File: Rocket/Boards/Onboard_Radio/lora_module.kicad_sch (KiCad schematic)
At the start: 30 parts, among them J11 RFIO SMA, U1 SX1262IMLTRT, U6 PE4259 RF Switch, Y2 Crystal

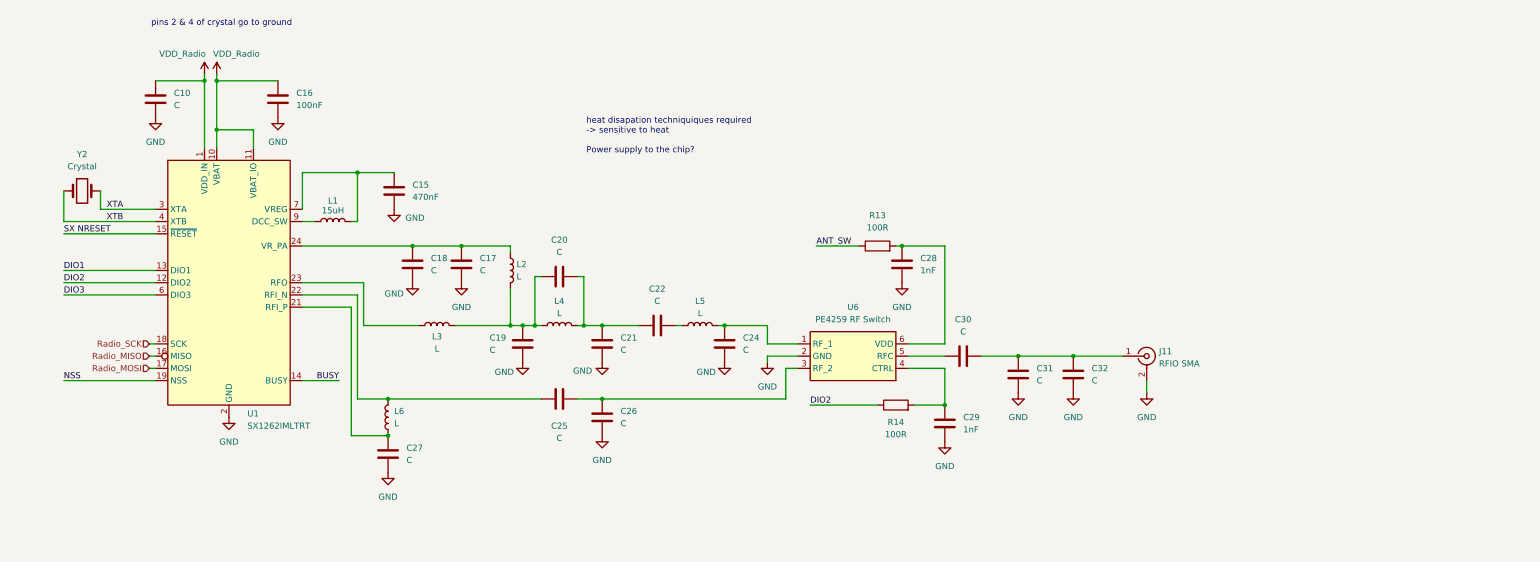
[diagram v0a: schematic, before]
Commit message: rf chip schematic changed
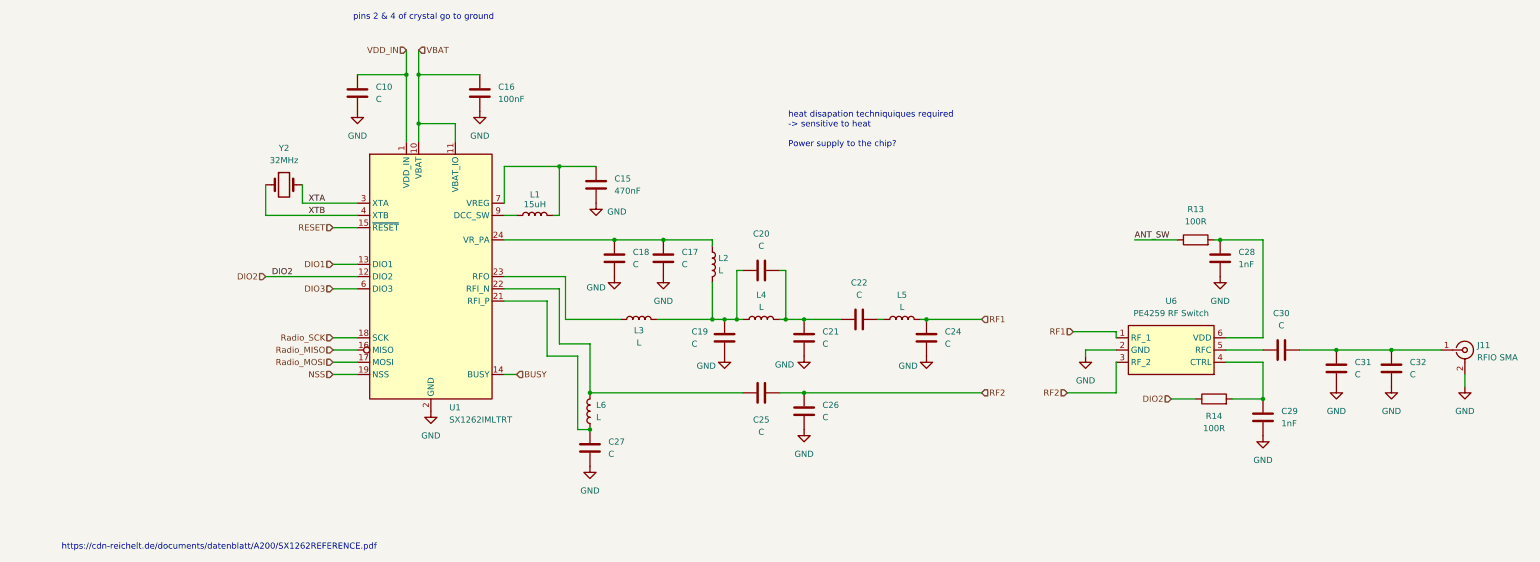
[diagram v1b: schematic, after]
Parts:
- Y2: value Crystal -> 32MHz
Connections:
- net RF1: now reaches C24.1, L5.2, U6.1 (RF_1)
- net RF2: now reaches C25.2, C26.2, U6.3 (RF_2)
- net SX NRESET renamed RESET
- net VDD_Radio renamed VBAT
- net VBAT: no longer C10.1, U1.1 (VDD_IN)
- new net VDD_IN: C10.1, U1.1 (VDD_IN)
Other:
- note added: "https://cdn-reichelt.de/documents/datenblatt/A200/SX1262REFERENCE.pdf"
- moved on the sheet: C10, C15, C16, C17, C18, C19, C20, C21, C22, C24, C25, C26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
